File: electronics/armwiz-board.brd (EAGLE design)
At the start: 125.7 x 114.3 mm, 94 parts, among them IC3 SN74LVC1G74DCT, J1 MICRO-SDCARD-CONNECTOR-330006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, J12 CORTEX_DEBUGSMD, Q1 DMP2035U-7, Q2 DMP2035U-7, Q3 DMN2075U-7, Q4 DMN2075U-7, Q5 DMP2035U-7, U1 STM32F10XRXT6, U2 APX809, U3 MCP73831, U4 MIC5219-3.3V, X1 FH12-12S-1S

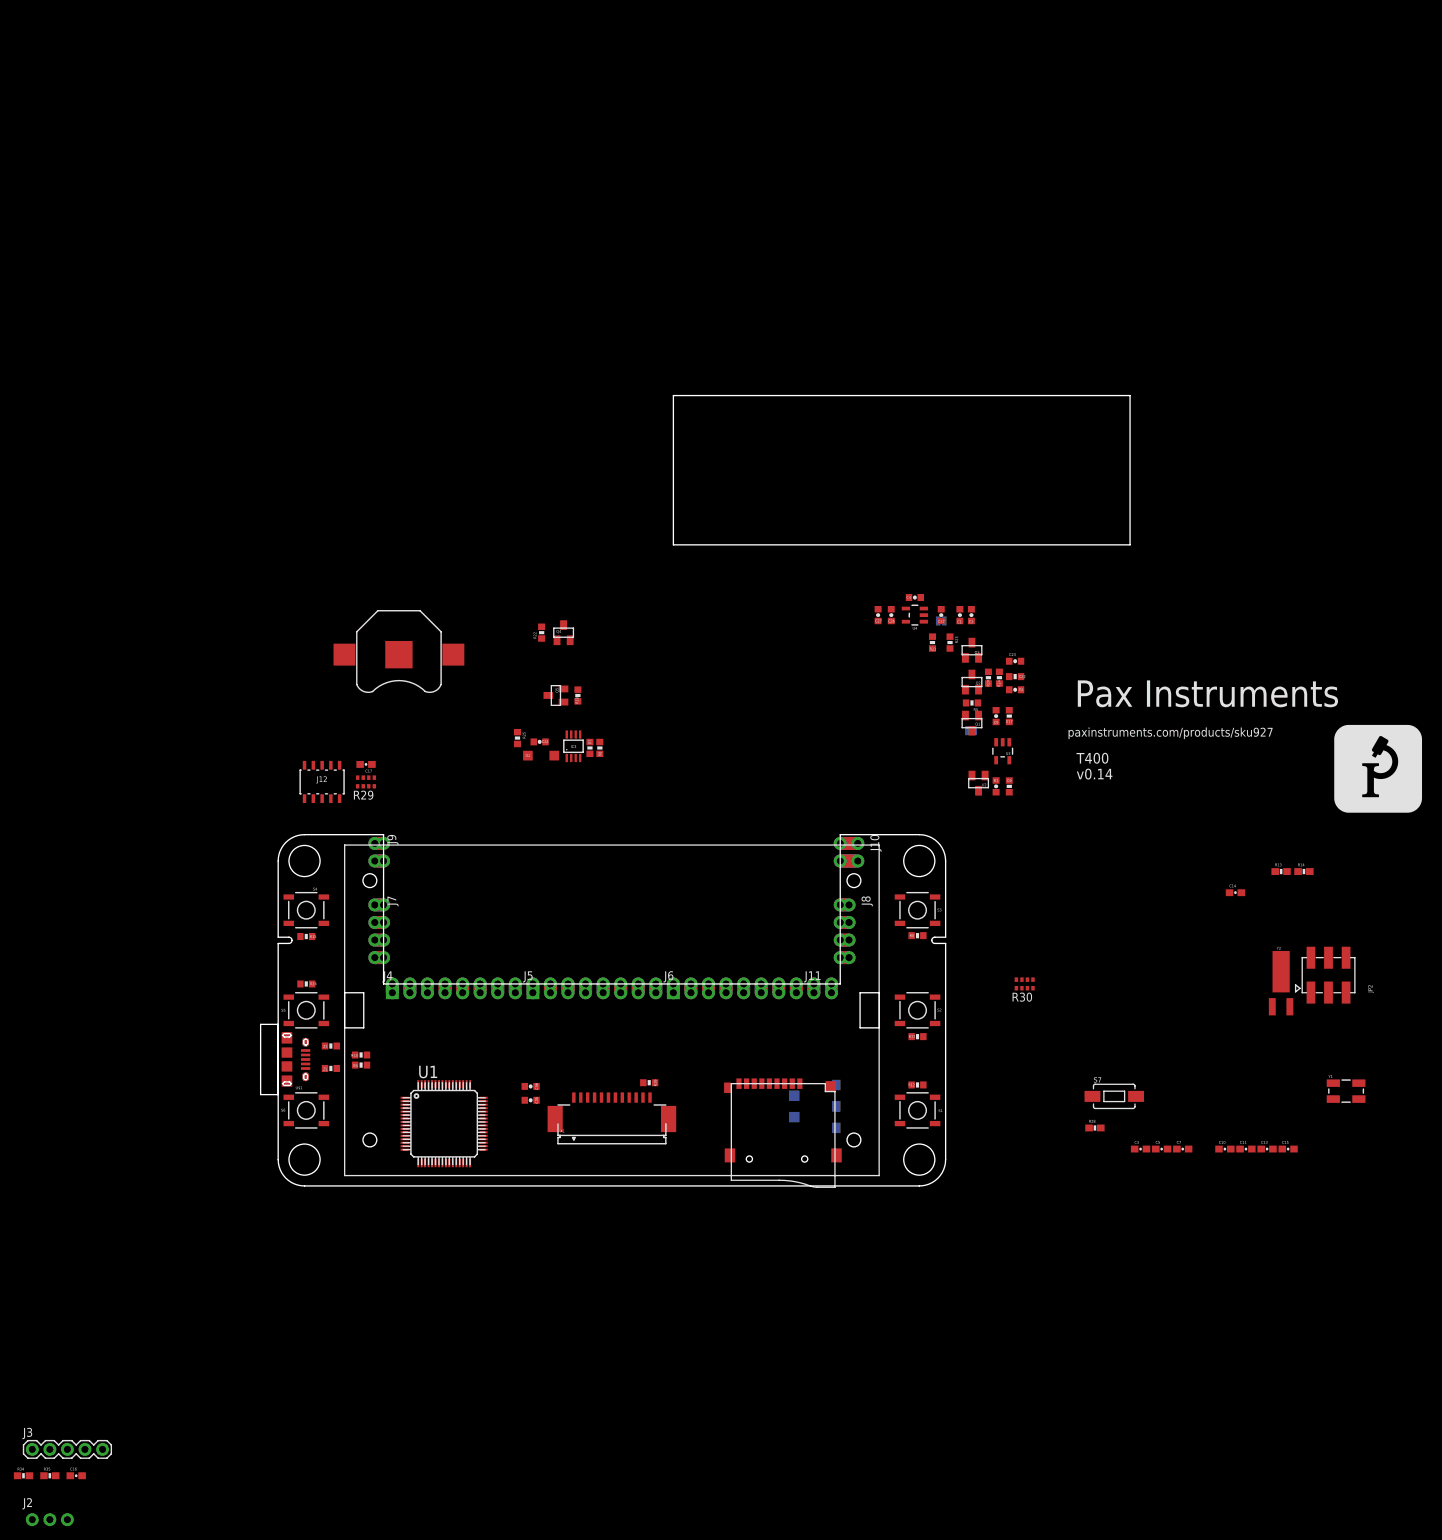
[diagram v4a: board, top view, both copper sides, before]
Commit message: Added some traces. Just starting layout to see the general areas things should be. Then I can determine where the LCD and other items should be connected to the MCU.
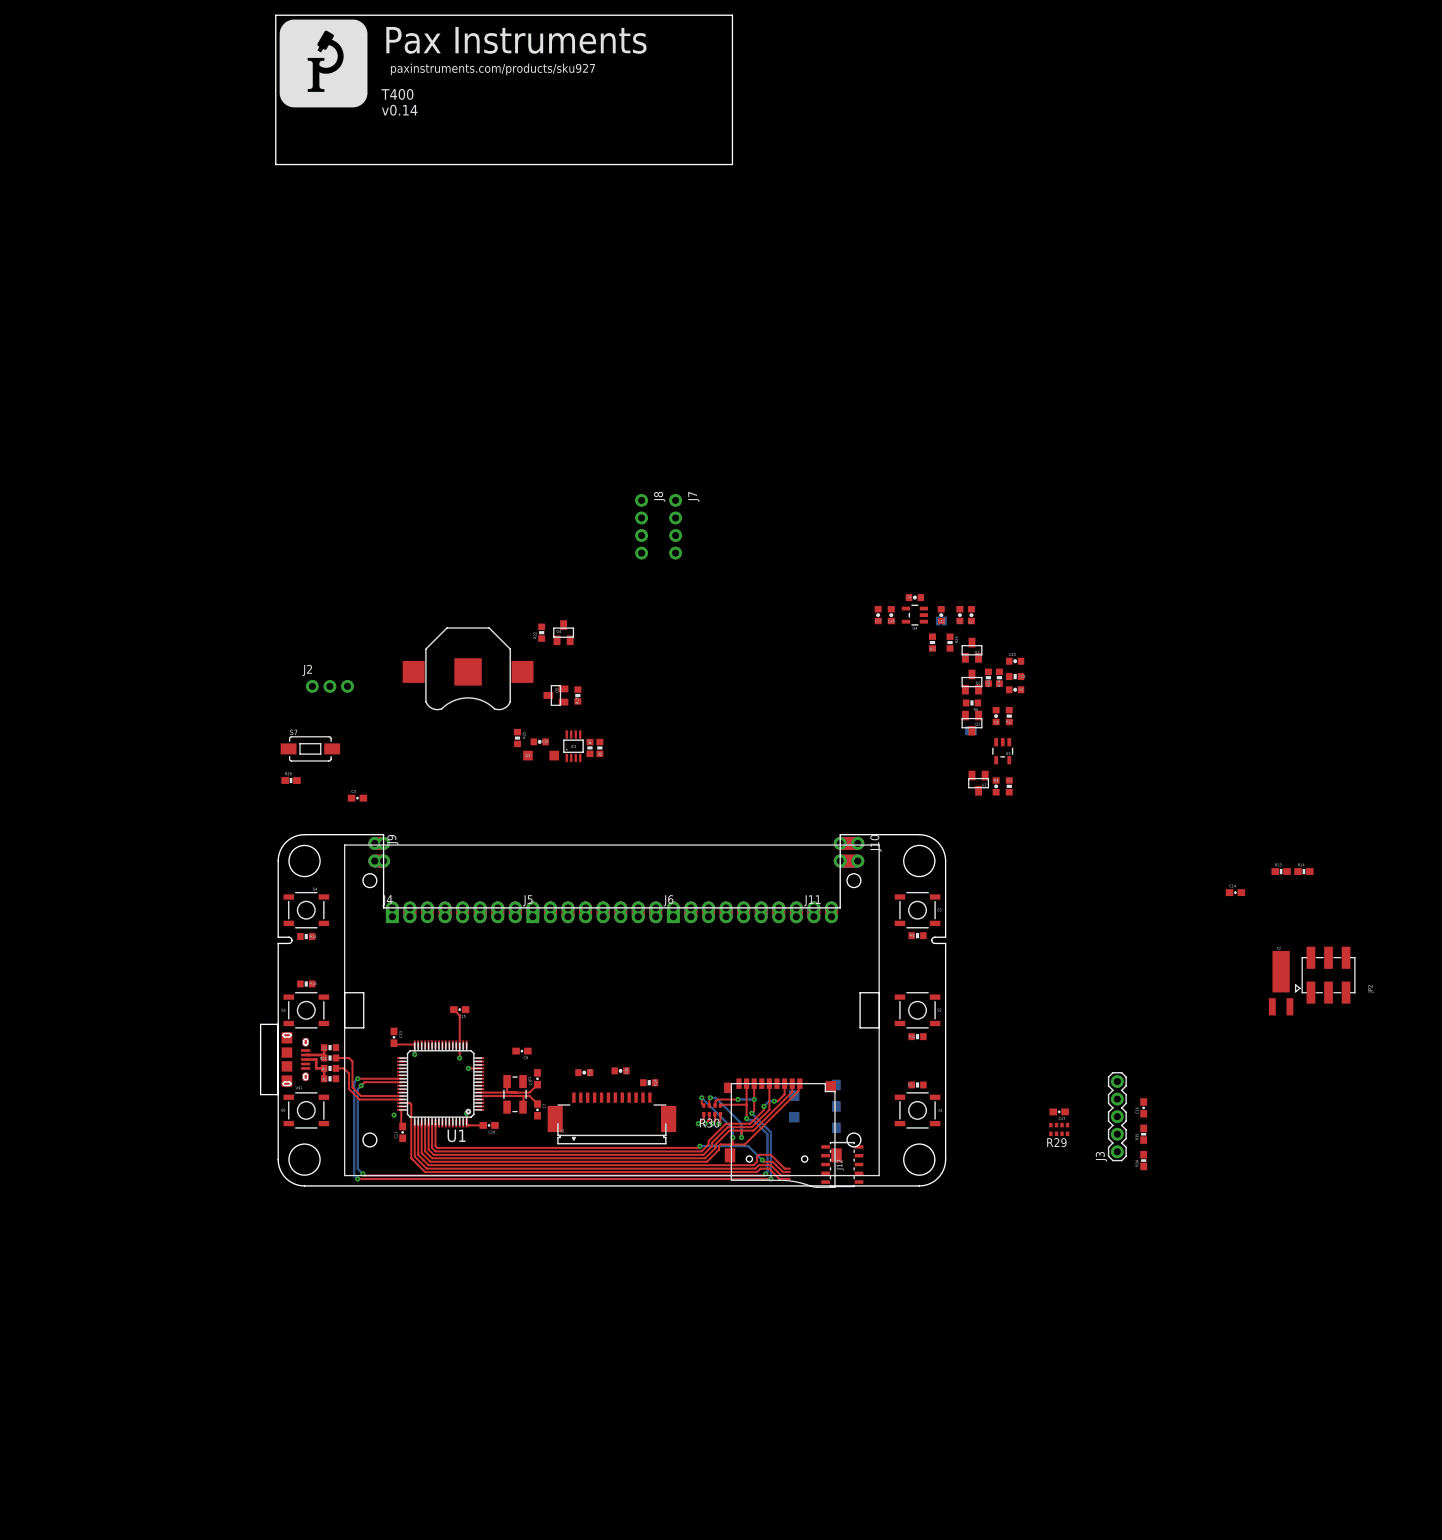
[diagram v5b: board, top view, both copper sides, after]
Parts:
- added C8: 0.1uF, SparkFun-Capacitors:0603-CAP
- moved U$6 183.5 mm to (0.22, 156.0)
- moved R34 168.3 mm to (125.2, 3.67), turned to 90 degrees
- moved R35 165.7 mm to (125.2, 7.48), turned to 90 degrees
- moved C16 163.3 mm to (125.2, 11.3), turned to 90 degrees
- moved J3 162.7 mm to (121.3, 4.94), turned to 90 degrees
- moved C13 127.3 mm to (16.8, 21.5), turned to 270 degrees
- moved J2 127.1 mm to (4.94, 72.2)
- moved R28 126.6 mm to (1.86, 58.6)
- moved S7 126.6 mm to (4.65, 63.2)
- moved C3 124.1 mm to (11.5, 56.1)
- moved C11 122.0 mm to (18.0, 7.75), turned to 90 degrees
- moved C15 121.5 mm to (26.2, 25.5), turned to 180 degrees
- moved Y1 120.2 mm to (34.2, 13.2), turned to 270 degrees
- moved C17 112.1 mm to (113.0, 10.7)
- moved R29 112.1 mm to (113.0, 8.17)
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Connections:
- net 3.3V: now also C8.2
- net GND: now also C8.1
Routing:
- net SDIO_D0: track 0.00 -> 102.4 mm, vias 0 -> 6
- net SDIO_D1: track 0.00 -> 96.9 mm, vias 0 -> 4
- net SDIO_D2: track 0.00 -> 74.8 mm, vias 0 -> 2
- net SDIO_D3: track 0.00 -> 73.3 mm, vias 0 -> 2
- net SWDIO: track 0.00 -> 65.7 mm
- net TDI: track 0.00 -> 60.8 mm
- net SWDCLK: track 0.00 -> 60.6 mm
- net SDIO_CMD: track 0.00 -> 60.3 mm, vias 0 -> 2
- net SDIO_CLK: track 0.00 -> 60.2 mm
- net SWO: track 0.00 -> 56.3 mm, vias 0 -> 2
- net 3.3V: track 0.00 -> 26.3 mm, vias 0 -> 9
- net USB-: track 0.00 -> 13.9 mm
- net USB+: track 0.00 -> 12.6 mm
- net N$5: track 0.00 -> 11.7 mm
- net N$11: track 0.00 -> 10.4 mm
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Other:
- board size 125.7 x 114.3 mm -> 99.1 x 169.3 mm

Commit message: Routing and layout.
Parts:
- removed BAT1: (no value), SparkFun-Electromechanical:BATTCON_12MM
- removed C16, C17: 0.1uF, SparkFun-Capacitors:0603-CAP
- removed J10, J9: (no value), SparkFun-Connectors:1X02_NO_SILK
- removed J12: CORTEX_DEBUGSMD, SparkFun-Connectors:SAMTECH_FTSH-105-01
- removed J3: (no value), SparkFun-Connectors:1X05
- removed J7, J8: (no value), SparkFun-Connectors:1X04_NO_SILK_ALL_ROUND
- removed R29: 10k, SparkFun-Passives:0603-ARV
- removed R34, R35: 10K, SparkFun-Resistors:0603-RES
- removed SJ1: JUMPER-PAD-2-NC_BY_TRACE, SparkFun-Passives:PAD-JUMPER-2-NC_BY_TRACE_YES_SILK
- removed Y2: (no value), SparkFun-FreqCtrl:CRYSTAL-32KHZ-SMD-MELF
- added C18: 0.1uF, SparkFun-Capacitors:0603-CAP
- added R2, R4: 10K, SparkFun-Resistors:0603-RES
- J2: device SparkFun-Connectors:1X03_NO_SILK -> SparkFun-Connectors:1X04
- moved C22 113.2 mm to (11.8, 10.0), turned to 90 degrees
- moved Q1 102.2 mm to (11.8, 16.0), turned to 90 degrees
- moved U3 101.5 mm to (12.9, 19.8), turned to 270 degrees
- moved U2 100.5 mm to (11.8, 12.5), turned to 90 degrees
- moved C6 98.1 mm to (15.8, 14.5), turned to 180 degrees
- moved R5 98.0 mm to (2.90, 80.8), turned to 270 degrees
- moved Q3 96.6 mm to (4.03, 85.1), turned to 90 degrees
- moved R20 95.0 mm to (7.96, 80.8)
- moved R24 94.3 mm to (10.3, 80.8)
- moved C23 94.1 mm to (12.6, 80.8), turned to 90 degrees
- moved Q2 92.5 mm to (8.63, 85.1), turned to 90 degrees
- moved R23 91.8 mm to (5.41, 80.8)
- moved R17 91.6 mm to (24.2, 26.2)
- moved R1 91.4 mm to (28.6, 26.1), turned to 270 degrees
- moved R3 89.5 mm to (22.0, 26.3)
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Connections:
- net TRST renamed MISO3
- removed net 5V: J3.5
- removed net MOSI: X1.6
- removed net N$10: SJ1.2, U$2.P$1
- removed net N$102: J8.4
- removed net N$104: J8.2
- removed net N$105: J8.1
- removed net N$108: J8.3
- removed net N$110: J10.1
- removed net N$112: J9.1
- removed net N$113: J9.2
- removed net N$114: J7.1
- removed net N$115: J7.2
- removed net N$116: J7.3
- removed net N$117: J7.4
- removed net N$15: U1.57
- removed net N$16: U1.58
- removed net N$17: U1.59
- removed net N$41: U1.61
- removed net N$42: U1.62
- removed net N$94: J10.2
- removed net RTC_BATT: BAT1.PWR@1, U1.1
- removed net RX1: J2.1, U1.43
- removed net SCK: X1.7
- removed net SWO: J12.6, R29.2, U1.55
- removed net TX1: J2.2, U1.42
- new net MOSI3: U1.57, X1.6
- new net SCK3: U1.55, X1.7
- net 3.3V: now also C18.2, J2.4, R4.2, U1.1; no longer C16.2, C17.2, J12.1, J3.4, R29.6, R29.7, R29.8, R35.2
- net GND: now also C18.1, J2.2, R2.2; no longer BAT1.GND, C16.1, C17.1, J12.3, J12.5, J12.9, J2.3, J3.2, R29.4, R34.2
- net LCD_A0: now also U1.62
- net LCD_BL: now also U1.58
- net LCD_CS: now also U1.59
- net LCD_RST: now also U1.61
- net NRST: no longer J12.10
- net RTC1: no longer Y2.X2
- net RTC2: no longer Y2.X1
- net SWDCLK: now also J2.3, R2.1; no longer J12.4, J3.3, R29.5, R34.1
- net SWDIO: now also J2.1, R4.1; no longer J12.2, J3.1, R29.1, R35.1
- net TDI: no longer J12.8, R29.3
- net VBAT: now also U$2.P$1; no longer SJ1.1
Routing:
- net VBAT: track 0.00 -> 69.4 mm
- net SWO: track 56.3 -> 0.00 mm, vias 2 -> 0
- net SWDCLK: track 60.6 -> 11.3 mm
- net LCD_BL: track 0.00 -> 45.0 mm, vias 0 -> 2
- net SWDIO: track 65.7 -> 23.3 mm
- net SCK3: track 0.00 -> 40.0 mm
- net LCD_CS: track 0.00 -> 37.8 mm, vias 0 -> 2
- net MOSI3: track 0.00 -> 37.4 mm
- net LCD_RST: track 0.00 -> 34.3 mm, vias 0 -> 2
- net LCD_A0: track 0.00 -> 31.9 mm, vias 0 -> 2
- net SDIO_D0: track 102.4 -> 72.3 mm, vias 6 -> 2
- net SDIO_D1: track 96.9 -> 69.5 mm, vias 4 -> 2
- net VBUS_IN: track 0.00 -> 23.3 mm
- net SDIO_CLK: track 60.2 -> 69.9 mm
- net USB+: track 12.6 -> 21.1 mm, vias 0 -> 2
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- added copper zone on layer 15, net 3.3V
- removed copper zone on layer 15, net GND
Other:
- outline, holes or cut-outs redrawn
- board text added: "3.3 regulator"
- board text added: "Battery Charging"
- board text added: "Battery detect"
- board text added: "Soft Power"
- board text removed: "Cortex Debug"

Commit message: More routing.
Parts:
- C1, C12, C2, C22, C23, C26, C27, C28, C35, C36, C4, C6, C9: device PaxInstrument-T400:SPARKFUN-CAPACITORS_0603-CAP -> resistor:C0402K
- C10, C11, C13, C14, C15, C18, C3, C5, C7, C8: device SparkFun-Capacitors:0603-CAP -> resistor:C0402K
- R1, R10, R11, R12, R15, R16, R17, R18, R19, R20, R21, R22, R23, R24, R25, R3, R5, R6, R7, R8, R9: device PaxInstrument-T400:SPARKFUN-RESISTORS_0603-RES -> resistor:R0402
- R13, R14, R2, R28, R4: device SparkFun-Resistors:0603-RES -> resistor:R0402
- moved C9 61.0 mm to (82.9, 2.81), turned to 270 degrees
- moved C28 34.5 mm to (50.5, 59.6)
- moved JP1 34.5 mm to (58.1, 62.7)
- moved Q4 34.5 mm to (57.3, 55.3)
- moved Q5 34.5 mm to (47.9, 55.2)
- moved R18 34.5 mm to (51.1, 55.2)
- moved R21 34.5 mm to (47.6, 59.6)
- moved R22 34.5 mm to (54.1, 55.3)
- moved R6 34.5 mm to (57.8, 59.6)
- moved R7 34.5 mm to (56.3, 59.6)
- moved IC3 34.5 mm to (54.0, 59.8)
- moved C23 27.3 mm to (19.1, 54.3)
- moved Q2 27.3 mm to (15.1, 58.6)
- moved Q3 27.3 mm to (10.5, 58.6)
- moved R20 27.3 mm to (14.5, 54.3)
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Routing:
- net VBAT: track 69.4 -> 3.35 mm
- net TDI: track 54.6 -> 0.00 mm, vias 1 -> 0
- net 3.3V: track 34.1 -> 2.12 mm, vias 10 -> 0
- net SWDIO: track 23.3 -> 0.00 mm
- net USB+: track 21.1 -> 0.00 mm, vias 2 -> 0
- net USB-: track 20.5 -> 0.00 mm, vias 2 -> 0
- net LCD_BL: track 45.0 -> 32.0 mm
- net SWDCLK: track 11.3 -> 0.00 mm
- net SCK3: track 40.0 -> 28.8 mm
- net MOSI3: track 37.4 -> 27.2 mm
- net LCD_CS: track 37.8 -> 27.7 mm
- net LCD_RST: track 34.3 -> 25.9 mm
- net SDIO_CLK: track 69.9 -> 61.6 mm, vias 0 -> 2
- net VBUS_IN: track 23.3 -> 15.7 mm
- net LCD_A0: track 31.9 -> 24.3 mm
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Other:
- board text removed: "Battery Charging"

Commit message: Unknown modification.
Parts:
- moved R2 1.00 mm to (14.0, 4.00), turned to 0 degrees
- moved R1 0.71 mm to (16.7, 5.67)
- moved C11 0.50 mm to (16.2, 9.75)
- moved R17 0.50 mm to (16.3, 8.47)
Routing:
- net VBAT: track 3.35 -> 84.6 mm, vias 0 -> 2
- net SWDIO: track 0.00 -> 19.8 mm
- net SWDCLK: track 0.00 -> 19.5 mm, vias 0 -> 2
- net USB+: track 0.00 -> 5.76 mm, vias 0 -> 1
- net SDIO_D0: track 72.8 -> 67.8 mm
- net USB-: track 0.00 -> 4.59 mm, vias 0 -> 1
- net SDIO_D1: track 66.9 -> 63.5 mm
